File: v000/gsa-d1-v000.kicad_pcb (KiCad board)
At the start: 2 copper layers, 85.7 x 49.5 mm, 21 parts, among them J501 CONN-4, J502 CONN-3, J503 CONN-2, J504 CONN-2, J505 CONN-2, J506 CONN-2, J507 CONN-2, J508 CONN-3

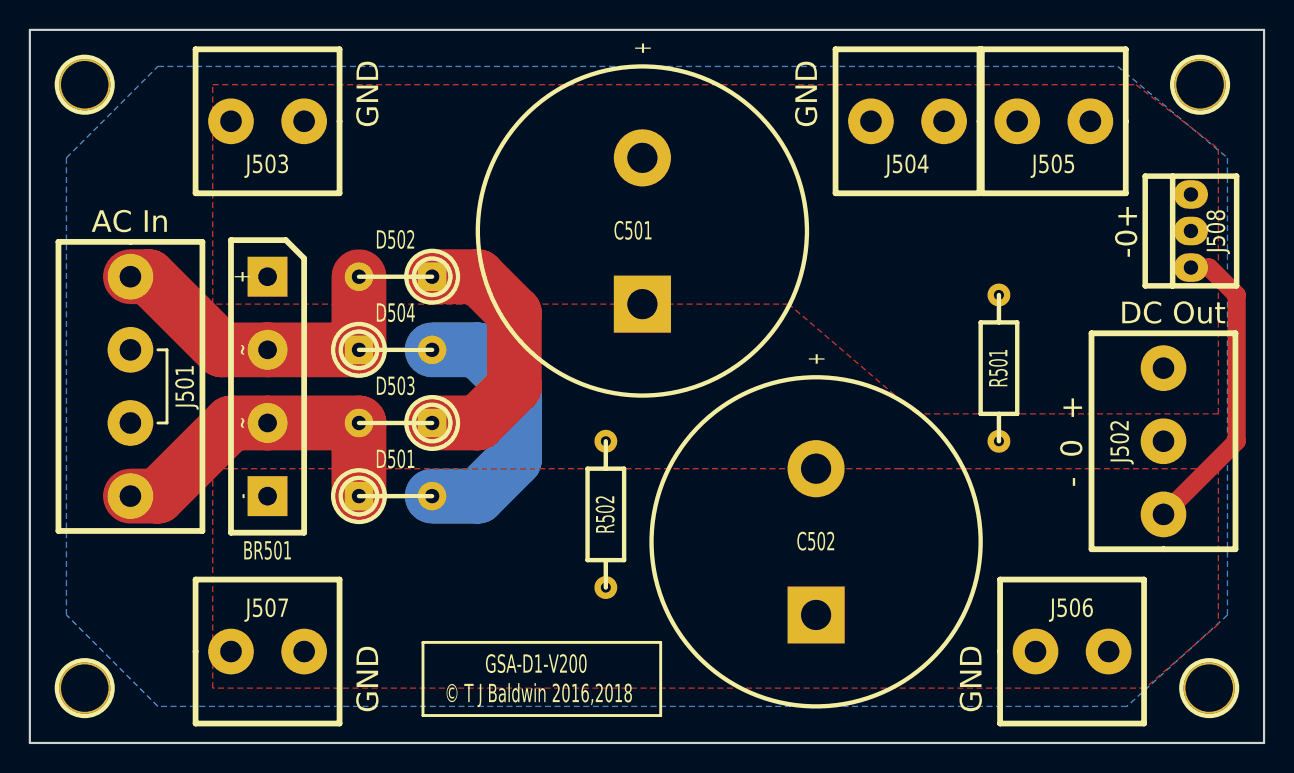
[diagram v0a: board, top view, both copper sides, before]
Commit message: Reduce size of power supply PCB
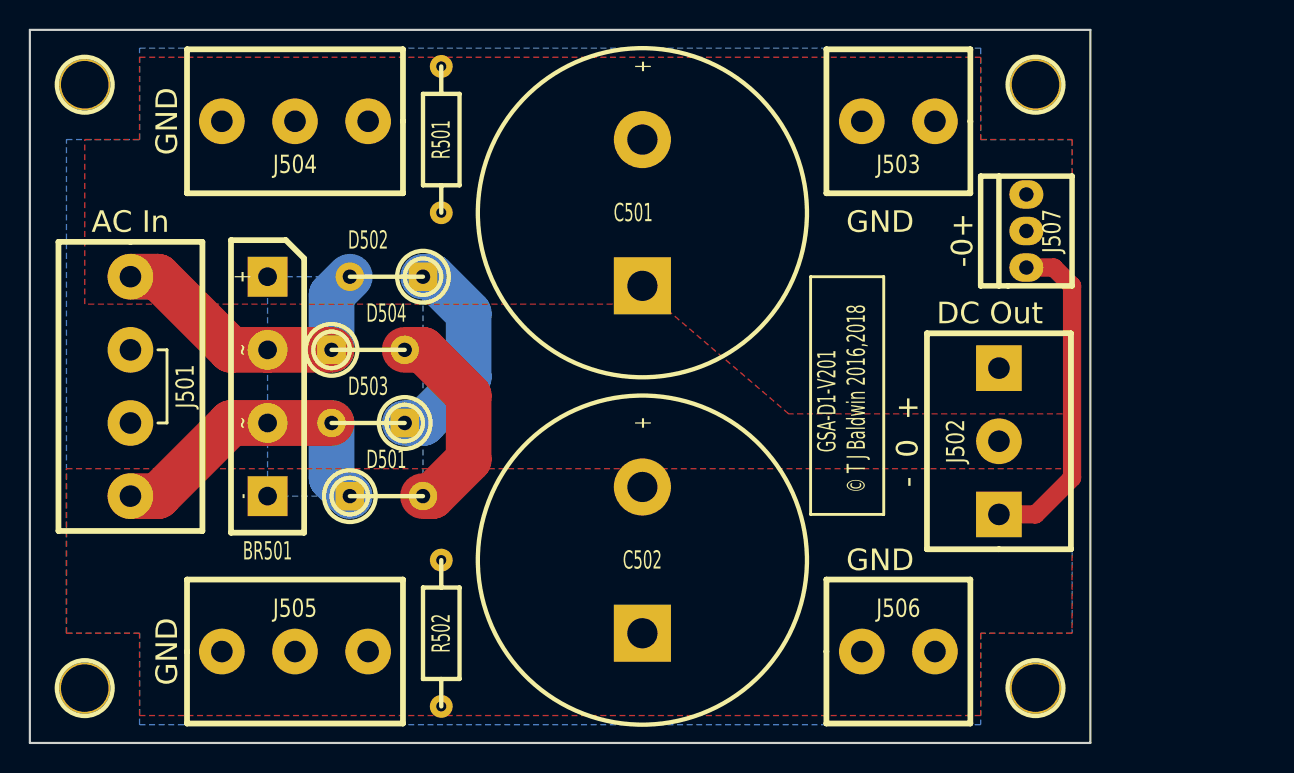
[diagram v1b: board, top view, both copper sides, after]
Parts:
- removed J508: CONN-3, gsa:MOLEX3
- J504, J505: value CONN-2 -> CONN-3; footprint gsa:SCREW2 -> gsa:SCREW3
- J507: value CONN-2 -> CONN-3; footprint gsa:SCREW2 -> gsa:MOLEX3
- moved J505 64.3 mm to (135.3, 121.3), turned to 0 degrees
- moved J507 60.3 mm to (186.1, 92.1), turned to 90 degrees
- moved J503 43.8 mm to (177.2, 84.5)
- moved J504 42.5 mm to (135.3, 84.5)
- moved R501 41.9 mm to (145.4, 85.7), turned to 270 degrees
- moved R502 14.1 mm to (145.4, 120.0), turned to 270 degrees
- moved C502 12.1 mm to (159.4, 114.9)
- moved H502 12.1 mm to (186.7, 123.8)
- moved J506 12.1 mm to (177.2, 121.3)
- moved H503 11.4 mm to (186.7, 81.9)
- moved J502 11.4 mm to (184.2, 106.7)
- moved D502 1.91 mm to (140.3, 100.3)
- moved D503 1.91 mm to (140.3, 105.4)
- moved C501 1.27 mm to (159.4, 90.8)
- moved D501 0.64 mm to (141.6, 110.5)
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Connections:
- J507 pad 1: GND -> /V-
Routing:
- net /V+: track 18.6 -> 14.4 mm
- net /V-: track 39.9 -> 37.0 mm
- net /AC1: track 23.1 -> 21.7 mm
- net /AC2: track 23.1 -> 21.7 mm
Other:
- board size 85.7 x 49.5 mm -> 73.7 x 49.5 mm
- board text added: "GSA-D1-V201 © T J Baldwin 2016,2018"
- board text removed: "GSA-D1-V200 © T J Baldwin 2016,2018"
